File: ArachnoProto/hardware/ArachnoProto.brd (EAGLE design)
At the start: 60.3 x 74.9 mm, 29 parts, among them J1 PINHEAD-17-REV, J2 PINHEAD-17-REV

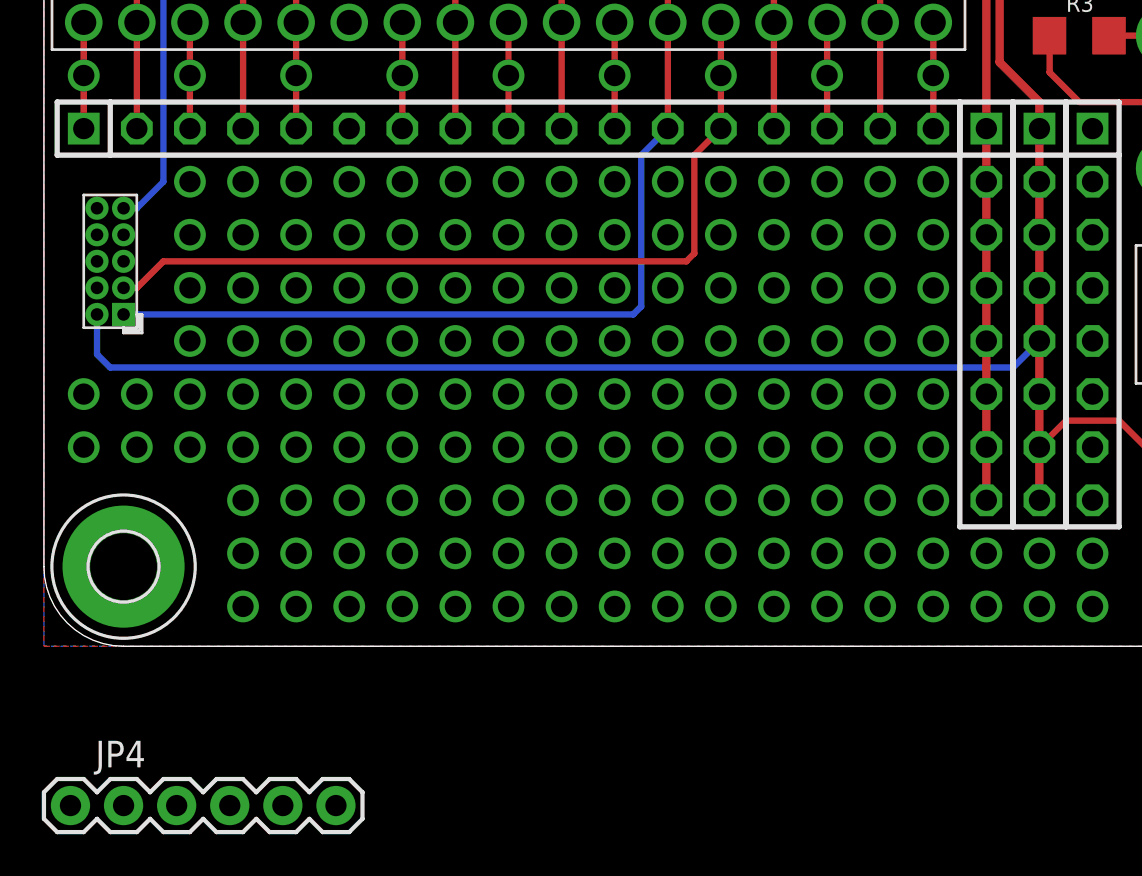
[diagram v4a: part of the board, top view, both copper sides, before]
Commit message: Modified ArachnNode to Arachnio Due standard
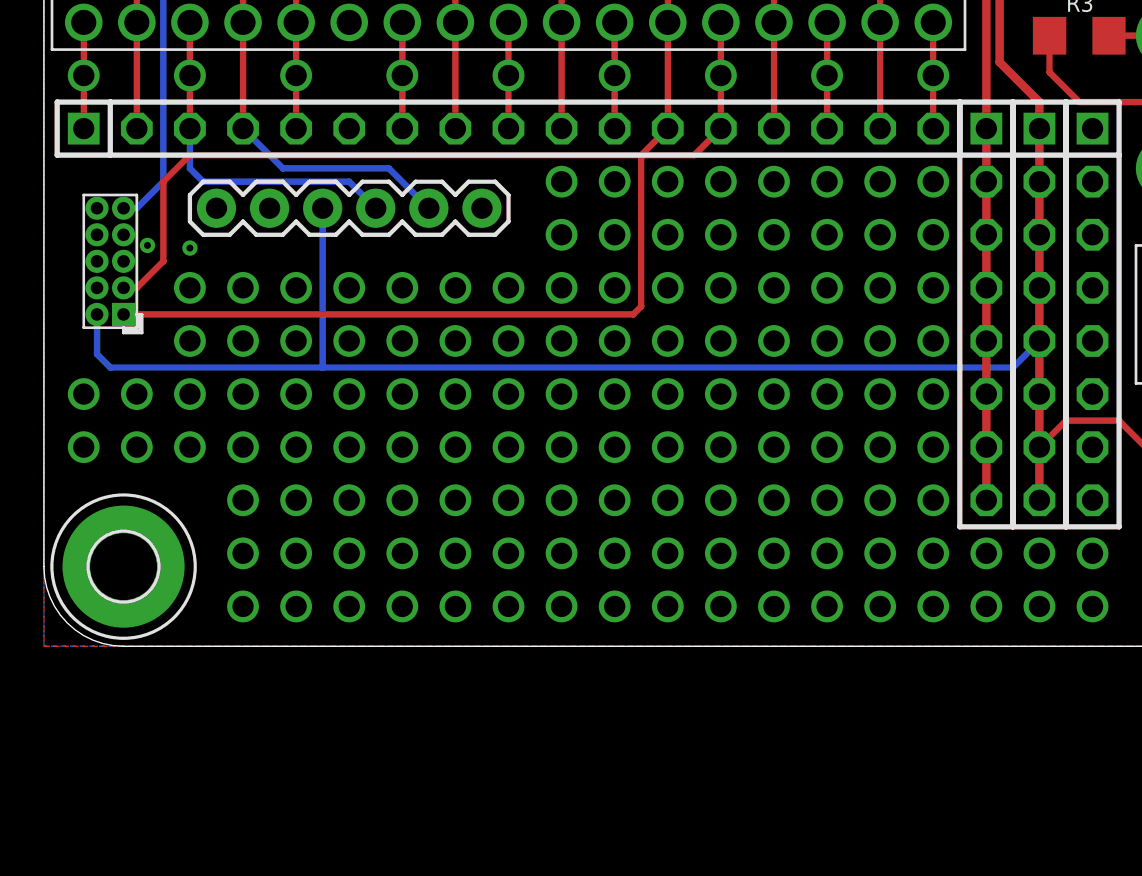
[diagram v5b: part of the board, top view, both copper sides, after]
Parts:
- moved JP4 34.7 mm to (21.0, 21.0), turned to 180 degrees
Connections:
- removed net N$354: JP4.RXI
- removed net N$355: JP4.TXO
- net D0: now also JP4.RXI
- net D1: now also JP4.TXO
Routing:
- net D1: track 5.08 -> 16.7 mm
- net D0: track 7.62 -> 18.1 mm
- net +3V3: track 139.4 -> 147.1 mm
- net IO8/SWCLK: track 39.6 -> 39.0 mm
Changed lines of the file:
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@@
 <element name="H4" library="holes" package="3,2-PAD" value="MOUNT-PAD-ROUND3.2" x="3.81" y="71.12"/>
 <element name="JP3" library="atmel-d21" package="PINHEAD_2X05_127" value="" x="3.175" y="18.415" rot="R180"/>
-<element name="JP4" library="SparkFun-Connectors" package="FTDI_BASIC" value="FTDI_BASICPTH" x="1.27" y="-7.62"/>
+<element name="JP4" library="SparkFun-Connectors" package="FTDI_BASIC" value="FTDI_BASICPTH" x="20.955" y="20.955" smashed="yes" rot="R180"/>
 </elements>
 <signals>
@@
 <wire x1="6.985" y1="29.845" x2="6.985" y2="27.305" width="0.3048" layer="1"/>
 <wire x1="6.985" y1="27.305" x2="6.985" y2="24.765" width="0.3048" layer="1"/>
+<contactref element="JP4" pad="TXO"/>
+<wire x1="15.875" y1="20.955" x2="14.605" y2="22.225" width="0.3048" layer="16"/>
+<wire x1="14.605" y1="22.225" x2="7.62" y2="22.225" width="0.3048" layer="16"/>
+<wire x1="7.62" y1="22.225" x2="6.985" y2="22.86" width="0.3048" layer="16"/>
+<wire x1="6.985" y1="22.86" x2="6.985" y2="24.765" width="0.3048" layer="16"/>
 </signal>
 <signal name="D0">
@@
 <wire x1="9.525" y1="24.765" x2="9.525" y2="29.845" width="0.3048" layer="1"/>
 <wire x1="9.525" y1="29.845" x2="9.525" y2="32.385" width="0.3048" layer="1"/>
+<contactref element="JP4" pad="RXI"/>
+<wire x1="18.415" y1="20.955" x2="16.51" y2="22.86" width="0.3048" layer="16"/>
+<wire x1="16.51" y1="22.86" x2="11.43" y2="22.86" width="0.3048" layer="16"/>
+<wire x1="11.43" y1="22.86" x2="9.525" y2="24.765" width="0.3048" layer="16"/>
 </signal>
 <signal name="SDA">
@@
 <contactref element="JP3" pad="6"/>
 <contactref element="JP4" pad="GND"/>
-<wire x1="50.165" y1="67.945" x2="56.515" y2="71.12" width="0" layer="19" extent="1-1"/>
-<wire x1="50.165" y1="65.405" x2="50.165" y2="67.945" width="0" layer="19" extent="1-1"/>
-<wire x1="50.165" y1="62.865" x2="50.165" y2="65.405" width="0" layer="19" extent="1-1"/>
-<wire x1="50.165" y1="60.325" x2="50.165" y2="62.865" width="0" layer="19" extent="1-1"/>
-<wire x1="50.165" y1="57.785" x2="50.165" y2="60.325" width="0" layer="19" extent="1-1"/>
-<wire x1="50.165" y1="55.245" x2="50.165" y2="57.785" width="0" layer="19" extent="1-1"/>
-<wire x1="50.165" y1="52.705" x2="50.165" y2="55.245" width="0" layer="19" extent="1-1"/>
-<wire x1="50.165" y1="50.165" x2="50.165" y2="52.705" width="0" layer="19" extent="1-1"/>
-<wire x1="56.995" y1="48.895" x2="50.165" y2="50.165" width="0" layer="19" extent="1-1"/>
-<wire x1="56.995" y1="26.035" x2="56.995" y2="48.895" width="0" layer="19" extent="1-1"/>
-<wire x1="50.165" y1="24.765" x2="56.995" y2="26.035" width="0" layer="19" extent="1-1"/>
-<wire x1="50.165" y1="22.225" x2="50.165" y2="24.765" width="0" layer="19" extent="1-1"/>
-<wire x1="50.165" y1="19.685" x2="50.165" y2="22.225" width="0" layer="19" extent="1-1"/>
-<wire x1="50.165" y1="17.145" x2="50.165" y2="19.685" width="0" layer="19" extent="1-1"/>
-<wire x1="50.165" y1="14.605" x2="50.165" y2="17.145" width="0" layer="19" extent="1-1"/>
-<wire x1="50.165" y1="12.065" x2="50.165" y2="14.605" width="0" layer="19" extent="1-1"/>
-<wire x1="50.165" y1="9.525" x2="50.165" y2="12.065" width="0" layer="19" extent="1-1"/>
-<wire x1="50.165" y1="6.985" x2="50.165" y2="9.525" width="0" layer="19" extent="1-1"/>
-<wire x1="56.515" y1="3.81" x2="50.165" y2="6.985" width="0" layer="19" extent="1-1"/>
-<wire x1="14.605" y1="24.765" x2="50.165" y2="24.765" width="0" layer="19" extent="1-1"/>
-<wire x1="14.605" y1="29.845" x2="14.605" y2="24.765" width="0" layer="19" extent="1-1"/>
-<wire x1="14.605" y1="32.385" x2="14.605" y2="29.845" width="0" layer="19" extent="1-1"/>
-<wire x1="2.54" y1="18.415" x2="14.605" y2="24.765" width="0" layer="19" extent="1-1"/>
-<wire x1="2.54" y1="17.145" x2="2.54" y2="18.415" width="0" layer="19" extent="1-1"/>
-<wire x1="3.81" y1="3.81" x2="2.54" y2="17.145" width="0" layer="19" extent="1-1"/>
-<wire x1="9.525" y1="45.085" x2="14.605" y2="32.385" width="0" layer="19" extent="1-1"/>
-<wire x1="9.525" y1="47.625" x2="9.525" y2="45.085" width="0" layer="19" extent="1-1"/>
-<wire x1="9.525" y1="50.165" x2="9.525" y2="47.625" width="0" layer="19" extent="1-1"/>
-<wire x1="13.97" y1="-7.62" x2="3.81" y2="3.81" width="0" layer="19" extent="1-1"/>
-<wire x1="3.81" y1="71.12" x2="9.525" y2="50.165" width="0" layer="19" extent="1-1"/>
+<via x="4.953" y="19.177" extent="1-16" drill="0.3302"/>
+<via x="6.985" y="19.05" extent="1-16" drill="0.3302"/>
 </signal>
 <signal name="+5V">
@@
 <wire x1="3.81" y1="17.145" x2="4.445" y2="17.145" width="0.3048" layer="1"/>
 <wire x1="4.445" y1="17.145" x2="5.715" y2="18.415" width="0.3048" layer="1"/>
-<wire x1="5.715" y1="18.415" x2="30.734" y2="18.415" width="0.3048" layer="1"/>
-<wire x1="30.734" y1="18.415" x2="31.115" y2="18.796" width="0.3048" layer="1"/>
-<wire x1="31.115" y1="18.796" x2="31.115" y2="23.495" width="0.3048" layer="1"/>
+<wire x1="5.715" y1="18.415" x2="5.715" y2="22.225" width="0.3048" layer="1"/>
+<wire x1="5.715" y1="22.225" x2="6.985" y2="23.495" width="0.3048" layer="1"/>
+<wire x1="6.985" y1="23.495" x2="31.115" y2="23.495" width="0.3048" layer="1"/>
 <wire x1="31.115" y1="23.495" x2="32.385" y2="24.765" width="0.3048" layer="1"/>
 </signal>
@@
 <wire x1="29.845" y1="29.845" x2="29.845" y2="32.385" width="0.3048" layer="1"/>
 <contactref element="JP3" pad="1"/>
-<wire x1="3.81" y1="15.875" x2="28.194" y2="15.875" width="0.3048" layer="16"/>
-<wire x1="28.194" y1="15.875" x2="28.575" y2="16.256" width="0.3048" layer="16"/>
-<wire x1="28.575" y1="16.256" x2="28.575" y2="23.495" width="0.3048" layer="16"/>
-<wire x1="28.575" y1="23.495" x2="29.845" y2="24.765" width="0.3048" layer="16"/>
+<wire x1="3.81" y1="15.875" x2="28.194" y2="15.875" width="0.3048" layer="1"/>
+<wire x1="28.194" y1="15.875" x2="28.575" y2="16.256" width="0.3048" layer="1"/>
+<wire x1="28.575" y1="16.256" x2="28.575" y2="23.495" width="0.3048" layer="1"/>
+<wire x1="28.575" y1="23.495" x2="29.845" y2="24.765" width="0.3048" layer="1"/>
 </signal>
 <signal name="TOUT">
@@
 <wire x1="47.625" y1="12.065" x2="47.625" y2="9.525" width="0.4064" layer="1"/>
 <wire x1="47.625" y1="9.525" x2="47.625" y2="6.985" width="0.4064" layer="1"/>
-<wire x1="3.175" y1="13.335" x2="46.355" y2="13.335" width="0.3048" layer="16"/>
+<wire x1="3.175" y1="13.335" x2="13.335" y2="13.335" width="0.3048" layer="16"/>
+<wire x1="13.335" y1="13.335" x2="46.355" y2="13.335" width="0.3048" layer="16"/>
 <wire x1="46.355" y1="13.335" x2="47.625" y2="14.605" width="0.3048" layer="16"/>
 <contactref element="R1" pad="2"/>
@@
 <wire x1="2.54" y1="13.97" x2="3.175" y2="13.335" width="0.3048" layer="16"/>
 <contactref element="JP4" pad="VCC"/>
-<wire x1="8.89" y1="-7.62" x2="3.175" y2="13.335" width="0" layer="19" extent="16-16"/>
-</signal>
-<signal name="N$9">
-<via x="6.985" y="22.225" extent="1-16" drill="1.016" shape="square"/>
-</signal>
-<signal name="N$10">
-<via x="9.525" y="22.225" extent="1-16" drill="1.016" shape="square"/>
-</signal>
-<signal name="N$11">
-<via x="12.065" y="22.225" extent="1-16" drill="1.016" shape="square"/>
-</signal>
-<signal name="N$12">
-<via x="14.605" y="22.225" extent="1-16" drill="1.016" shape="square"/>
-</signal>
-<signal name="N$13">
-<via x="17.145" y="22.225" extent="1-16" drill="1.016" shape="square"/>
-</signal>
-<signal name="N$14">
-<via x="19.685" y="22.225" extent="1-16" drill="1.016" shape="square"/>
-</signal>
-<signal name="N$15">
-<via x="22.225" y="22.225" extent="1-16" drill="1.016" shape="square"/>
+<wire x1="13.335" y1="20.955" x2="13.335" y2="13.335" width="0.3048" layer="16"/>
 </signal>
 <signal name="N$16">
@@
 <signal name="N$23">
 <via x="42.545" y="22.225" extent="1-16" drill="1.016" shape="square"/>
-</signal>
-<signal name="N$24">
-<via x="6.985" y="19.685" extent="1-16" drill="1.016" shape="square"/>
-</signal>
-<signal name="N$25">
-<via x="9.525" y="19.685" extent="1-16" drill="1.016" shape="square"/>
-</signal>
-<signal name="N$26">
-<via x="12.065" y="19.685" extent="1-16" drill="1.016" shape="square"/>
-</signal>
-<signal name="N$27">
-<via x="14.605" y="19.685" extent="1-16" drill="1.016" shape="square"/>
-</signal>
-<signal name="N$28">
-<via x="17.145" y="19.685" extent="1-16" drill="1.016" shape="square"/>
-</signal>
-<signal name="N$29">
-<via x="19.685" y="19.685" extent="1-16" drill="1.016" shape="square"/>
-</signal>
-<signal name="N$30">
-<via x="22.225" y="19.685" extent="1-16" drill="1.016" shape="square"/>
 </signal>
 <signal name="N$31">
@@
 <via x="50.165" y="70.485" extent="1-16" drill="1.016" shape="square"/>
 </signal>
-<signal name="N$354">
-<contactref element="JP4" pad="RXI"/>
-</signal>
-<signal name="N$355">
-<contactref element="JP4" pad="TXO"/>
-</signal>
 </signals>

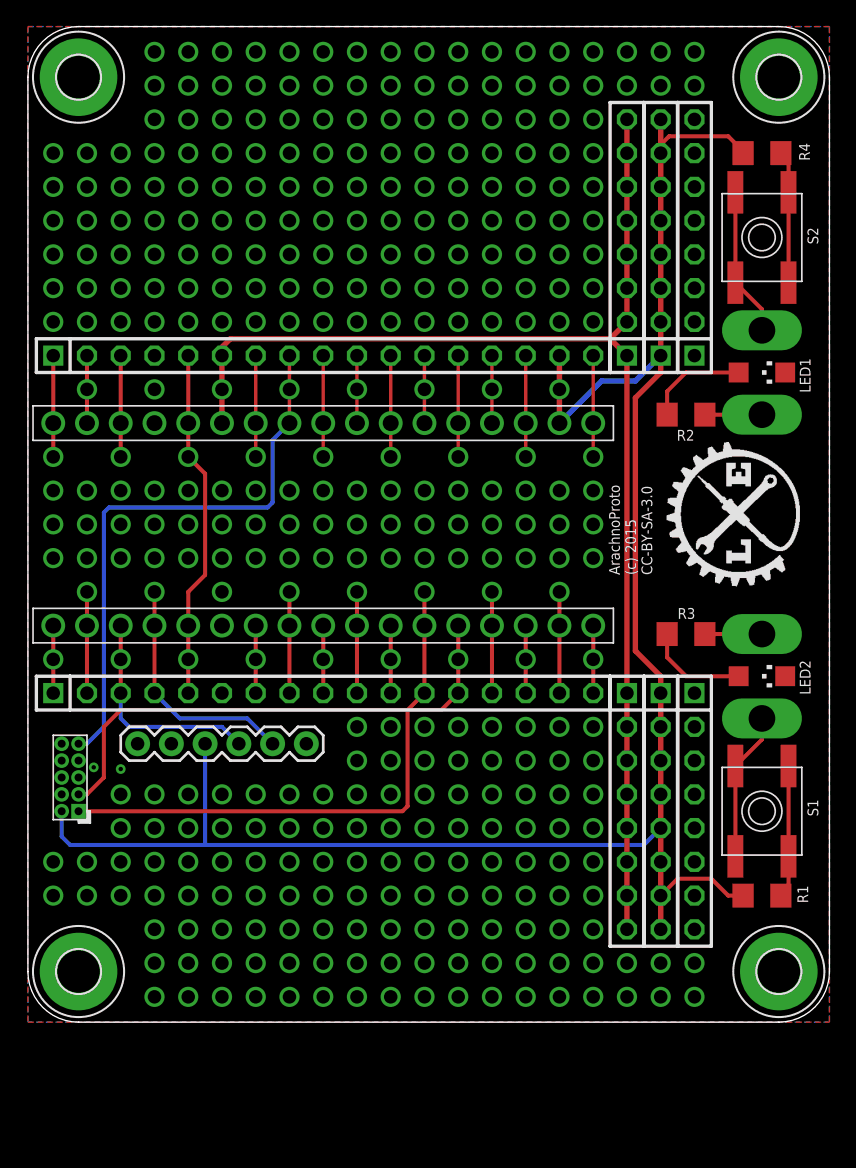
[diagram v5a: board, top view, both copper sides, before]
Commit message: Updated Arachnoproto with fixed SWD header.
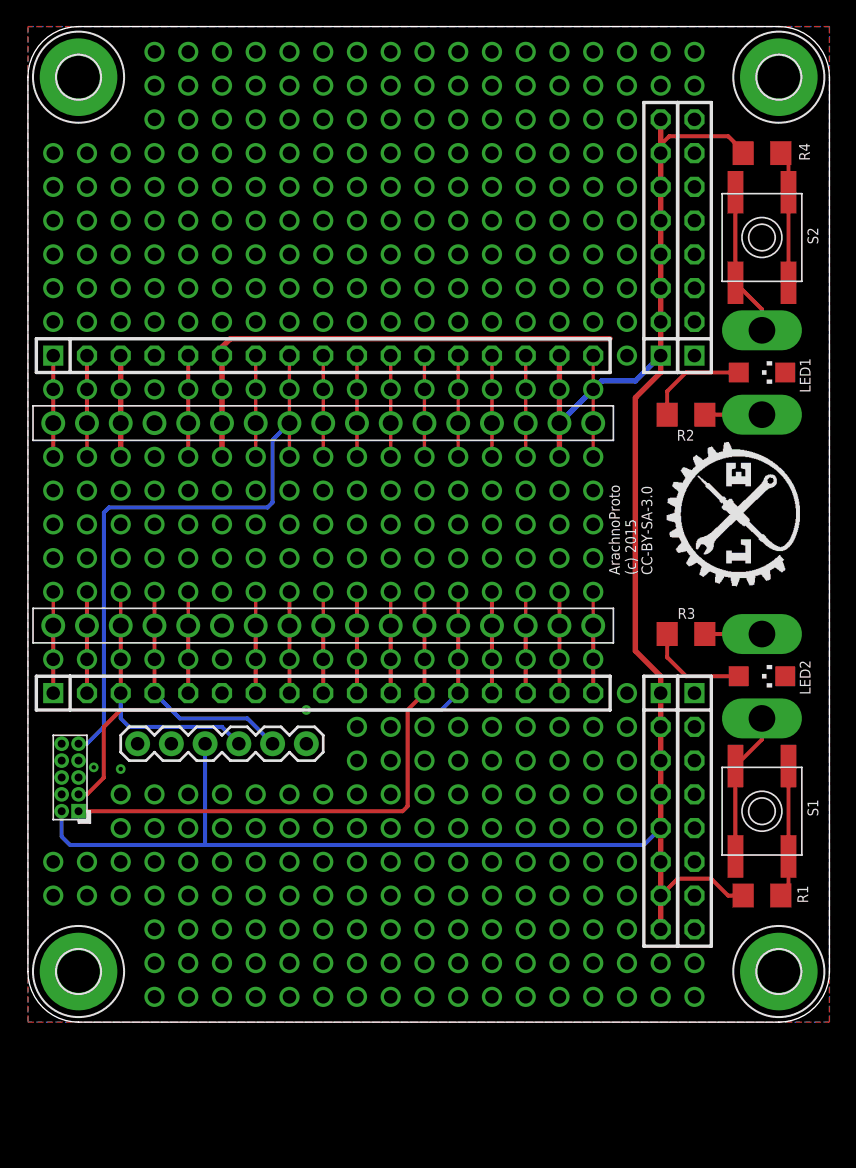
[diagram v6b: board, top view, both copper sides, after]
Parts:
- removed JP20, JP21: (no value), pinhead:1X08
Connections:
- removed net +5V: J2.23, J2.6, JP2.6, JP20.1, JP20.2, JP20.3, JP20.4, JP20.5, JP20.6, JP20.7, JP20.8, JP21.1, JP21.2, JP21.3, JP21.4, JP21.5, JP21.6, JP21.7, JP21.8
- removed net N$2: J1.17, J1.34, JP1.17
- removed net N$4: J2.17, J2.34, JP2.17
- removed net TOUT: J2.24, J2.7, JP2.7
- new net ERASE: J2.24, J2.41, J2.7, JP2.7
- new net IO12: J1.17, J1.34, J1.51, JP1.17
- new net IO13: J2.17, J2.34, J2.51, JP2.17
- new net SWO/IO14: J2.25, J2.42, J2.8, JP2.8, JP3.9
- new net VCC: J2.23, J2.40, J2.6, JP2.6
- net +3V3: now also J2.50
- net A0: now also J2.48
- net A1: now also J2.47
- net A2: now also J2.46
- net A3: now also J2.45
- net A4: now also J2.44
- net A5: now also J2.43
- net AREF: now also J2.49
- net D0: now also J1.38
- net D1: now also J1.37
- net D4: now also J1.43
- net D5: now also J1.44
- net D6: now also J1.45
- net D7/SWDIO: now also J1.46
- net ESP_RST: now also J2.22, J2.39, J2.5, JP2.5; no longer J2.25, J2.8, JP2.8, JP3.9
- net GND: now also J1.40, J2.38
- net IO10: now also J1.49
- net IO11: now also J1.50
- net IO8/SWCLK: now also J1.47
- net IO9: now also J1.48
- net MISO: now also J2.36
- net MOSI: now also J1.35
- net RESET: now also J1.39; no longer J2.22, J2.5, JP2.5
- net SCK: now also J2.35
- net SCL: now also J1.42
- net SDA: now also J1.41
- net SS: now also J1.36
- net VIN: now also J2.37
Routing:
- net +5V: track 97.2 -> 0.00 mm
- net SWO/IO14: track 0.00 -> 45.7 mm
- net VCC: track 0.00 -> 37.7 mm
- net ESP_RST: track 43.2 -> 7.62 mm
- net RESET: track 26.5 -> 7.62 mm
- net TOUT: track 7.62 -> 0.00 mm
- net N$4: track 7.62 -> 0.00 mm, vias 0 -> 1
- net IO13: track 0.00 -> 7.62 mm
- net IO12: track 0.00 -> 7.62 mm
- net ERASE: track 0.00 -> 7.62 mm
- net N$2: track 5.08 -> 0.00 mm, vias 0 -> 1
- net D1: track 16.7 -> 20.1 mm
- net SDA: track 5.08 -> 7.62 mm
- net MOSI: track 5.08 -> 7.62 mm
- net MISO: track 5.08 -> 7.62 mm
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
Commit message: Fixed broken debug port
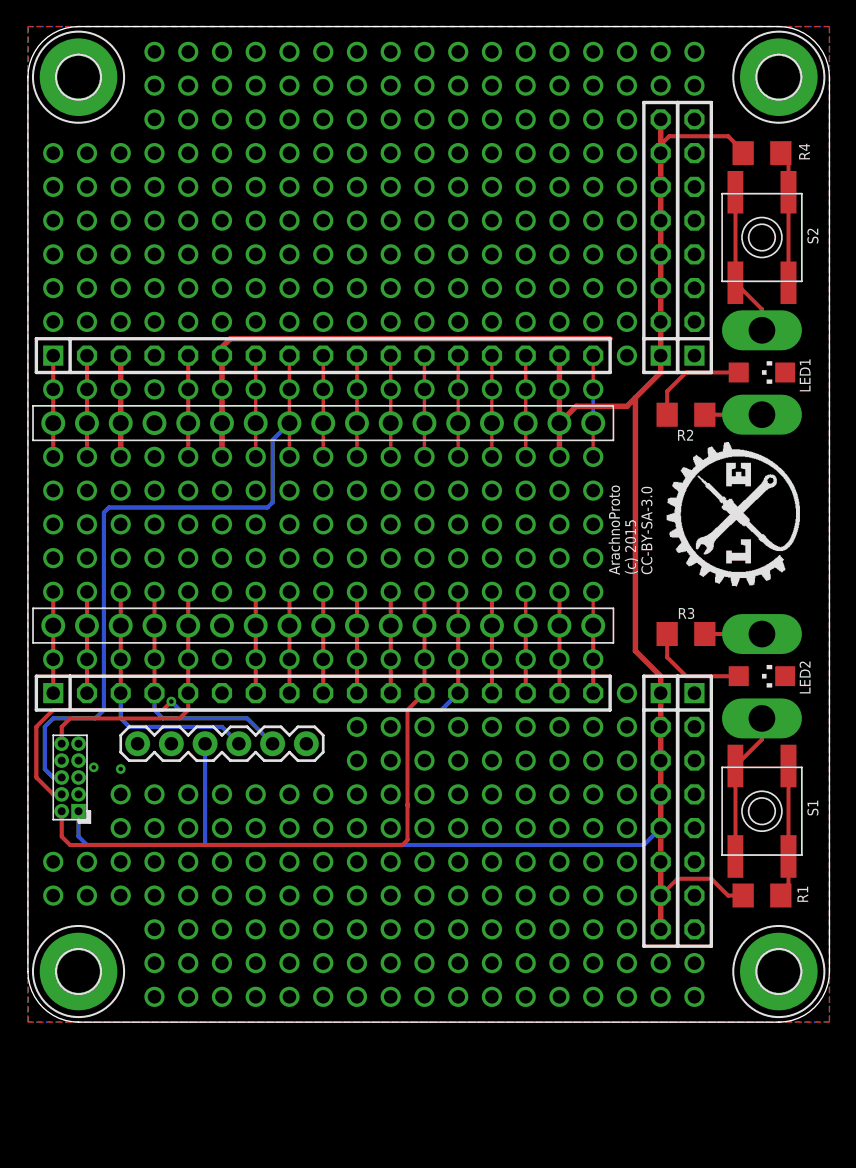
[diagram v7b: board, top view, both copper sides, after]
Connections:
- net +3V3: now also JP3.1; no longer JP3.2
- net D7/SWDIO: now also JP3.2; no longer JP3.1
- net GND: now also JP3.3, JP3.5, JP3.9; no longer JP3.4, JP3.6
- net IO8/SWCLK: now also JP3.4; no longer JP3.3
- net RESET: now also JP3.10
- net SWO/IO14: now also JP3.6; no longer JP3.9
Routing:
- net RESET: track 7.62 -> 20.2 mm
- net D7/SWDIO: track 41.6 -> 47.7 mm
- net SWO/IO14: track 45.7 -> 51.7 mm
- net IO8/SWCLK: track 41.6 -> 47.2 mm
- net +3V3: track 149.6 -> 145.1 mm
- net D0: track 18.1 -> 18.8 mm
